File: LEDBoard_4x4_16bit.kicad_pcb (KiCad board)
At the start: 2 copper layers, 39.5 x 39.5 mm, 35 parts, among them J1 signal_in, J2 power, J6 signal_out, U1 TLC5971PWPR, U2 TLC5971PWPR, U3 TLC5971PWPR, U4 TLC5971PWPR

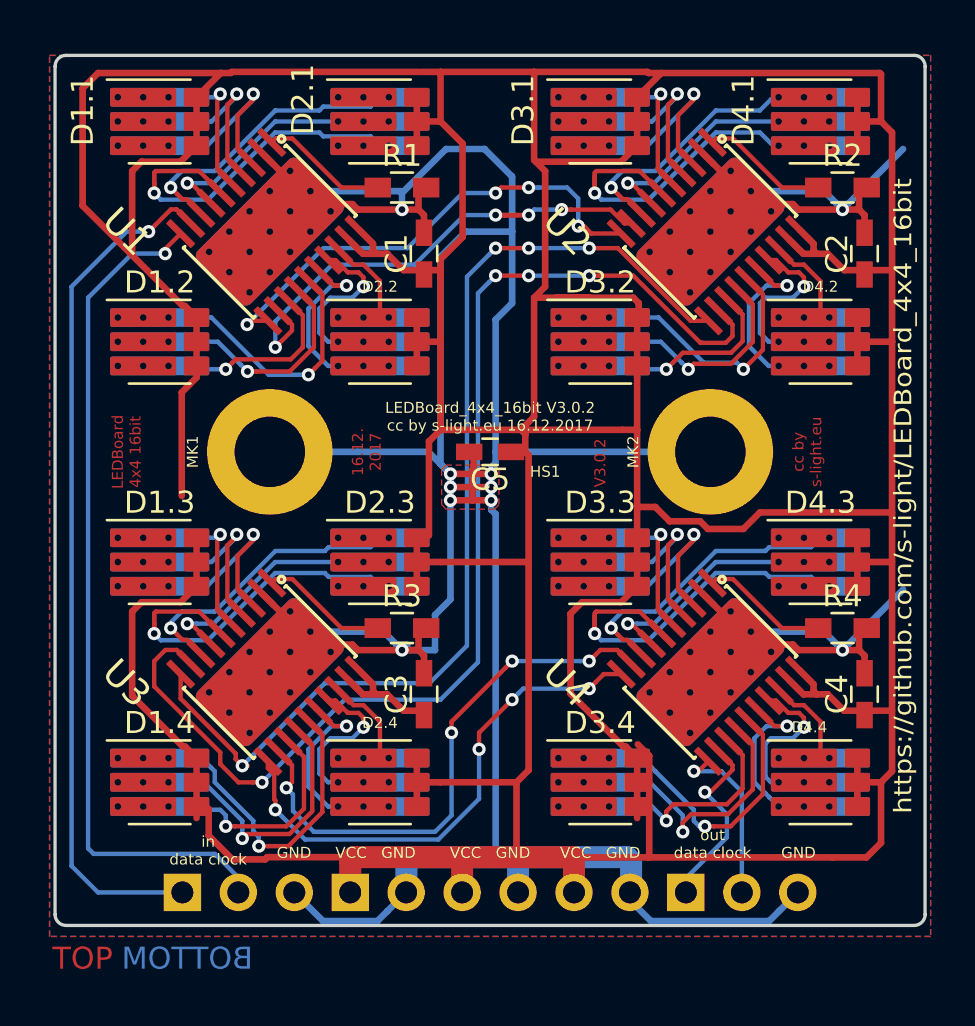
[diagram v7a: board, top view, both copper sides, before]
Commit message: update Schematics & PCB to - kicad nightliy 599 - use current default librarie symbols and footprints - create renderings
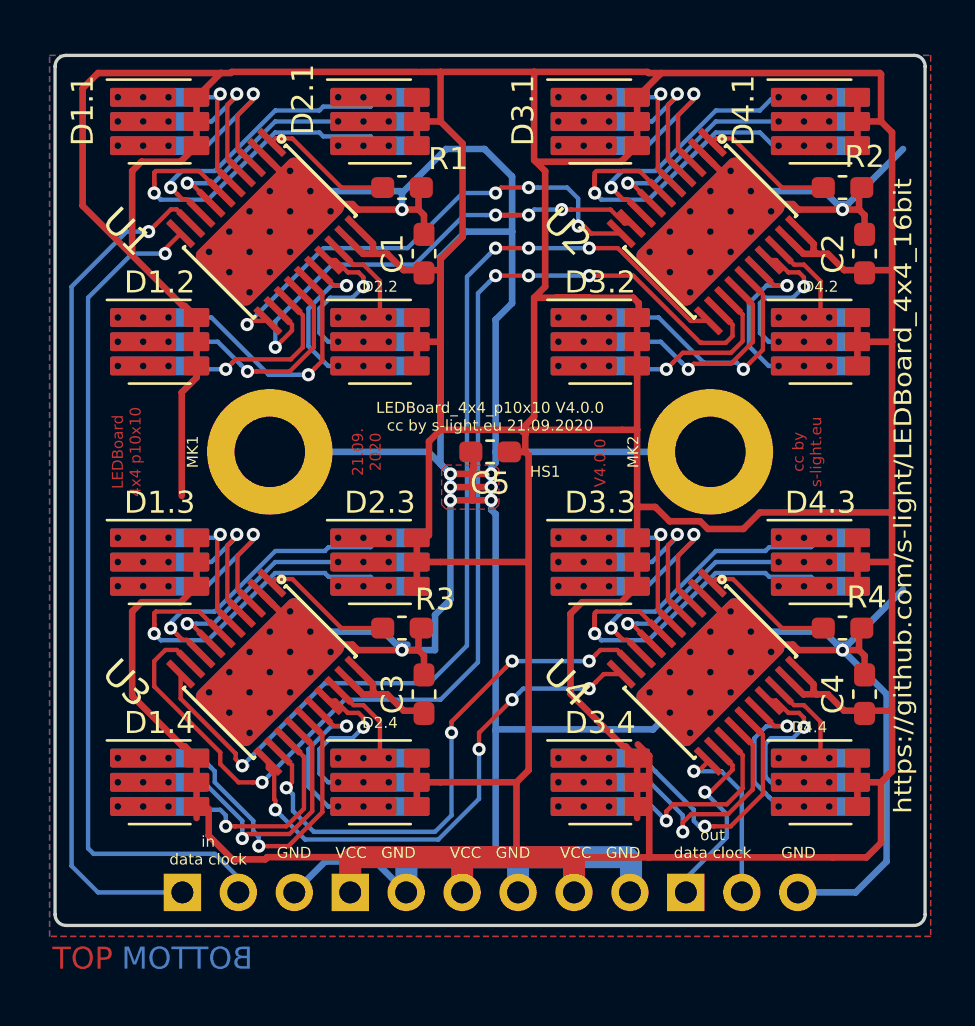
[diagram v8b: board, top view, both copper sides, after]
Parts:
- C1, C2, C3, C4, C5: footprint Capacitors_SMD:C_0603_HandSoldering -> Capacitor_SMD:C_0603_1608Metric_Pad1.05x0.95mm_HandSolder
- J1, J6: footprint Socket_Strips:Socket_Strip_Straight_1x03_Pitch2.54mm -> Connector_PinSocket_2.54mm:PinSocket_1x03_P2.54mm_Vertical
- J2: footprint Socket_Strips:Socket_Strip_Straight_1x06_Pitch2.54mm -> Connector_PinSocket_2.54mm:PinSocket_1x06_P2.54mm_Vertical
- R1, R2, R3, R4: footprint Resistors_SMD:R_0603_HandSoldering -> Resistor_SMD:R_0603_1608Metric_Pad1.05x0.95mm_HandSolder
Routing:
- net GND: track 187.1 -> 204.5 mm
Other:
- net class Default removed
- net class LED removed
- net class Power removed
- net class signal removed
- board text added: "21.09. 2020"
- board text added: "LEDBoard 4x4 p10x10"
- board text added: "LEDBoard_4x4_p10x10 V4.0.0 cc by s-light.eu 21.09.2020"
- board text added: "V4.0.0"
- board text removed: "16.12. 2017"
- board text removed: "LEDBoard 4x4 16bit"
- board text removed: "LEDBoard_4x4_16bit V3.0.2 cc by s-light.eu 16.12.2017"
- board text removed: "V3.0.2"
